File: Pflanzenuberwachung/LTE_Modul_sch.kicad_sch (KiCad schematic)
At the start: 22 parts, among them IC1 2615011136000, IC2 SN74AVC4T245PWR, J1 Antennen Anschluss, J2 Nano Sim, Q1 BSS138, SW1 CK_KMS2xxG

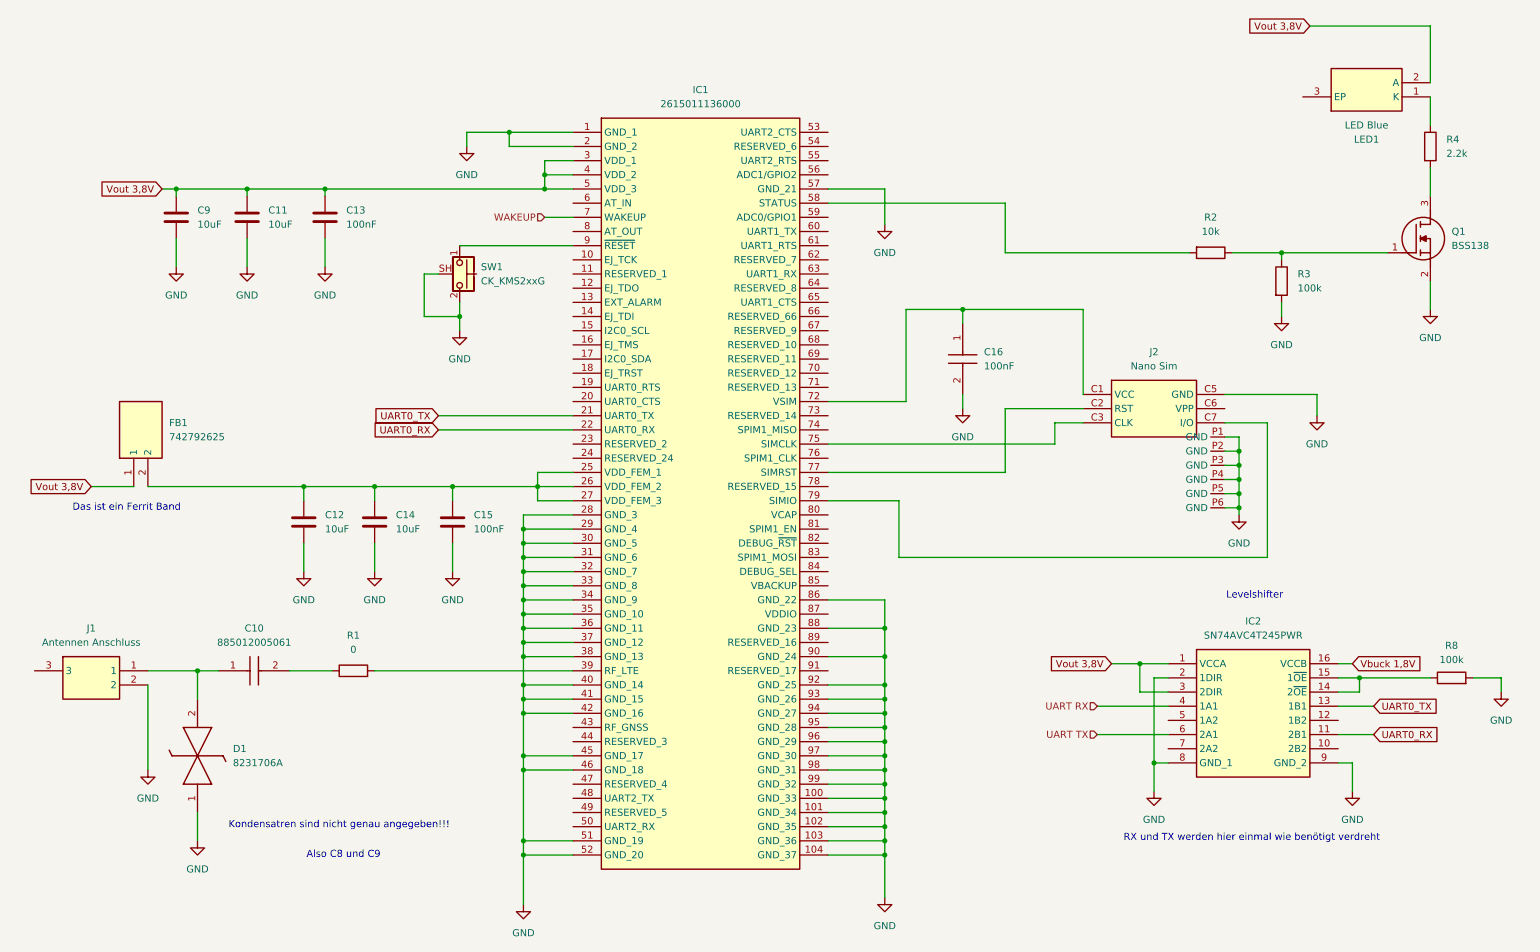
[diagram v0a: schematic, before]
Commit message: PCB Bord
PCB Design und kleiner nicht relevante änderungen
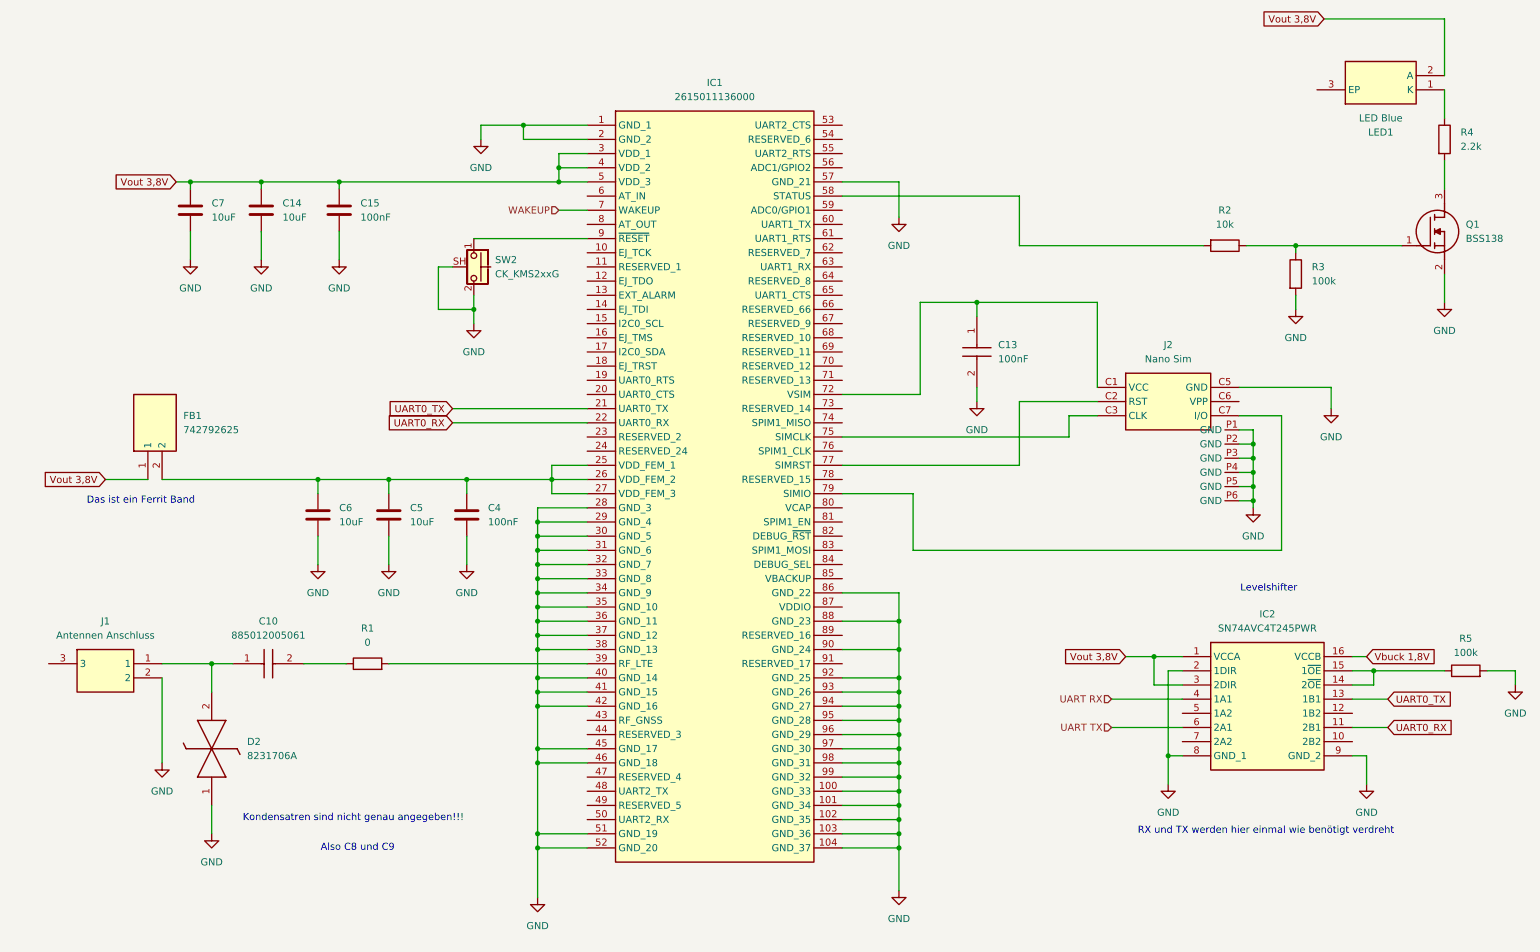
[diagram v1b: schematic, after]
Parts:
- removed C11, C12, C9: 10uF, Capacitor_SMD:C_0805_2012Metric, symbol Device:C
- removed C13: 100nF, Capacitor_SMD:C_0805_2012Metric, symbol Device:C
- removed C16: 100nF, Capacitor_SMD:C_0805_2012Metric, symbol Bauteile2:885012205037
- removed D1: 8231706A, DIONC1005X60N, symbol Bauteile2:8231706A
- removed R8: 100k, Resistor_SMD:R_0805_2012Metric, symbol Device:R
- removed SW1: CK_KMS2xxG, Button_Switch_SMD:SW_SPST_CK_KMS2xxGP, symbol Switch:CK_KMS2xxG
- added C13: 100nF, Capacitor_SMD:C_0805_2012Metric, symbol Bauteile2:885012205037
- added C4: 100nF, Capacitor_SMD:C_0805_2012Metric, symbol Device:C
- added C5, C6, C7: 10uF, Capacitor_SMD:C_0805_2012Metric, symbol Device:C
- added D2: 8231706A, DIONC1005X60N, symbol Bauteile2:8231706A
- added R5: 100k, Resistor_SMD:R_0805_2012Metric, symbol Device:R
- added SW2: CK_KMS2xxG, Button_Switch_SMD:SW_SPST_CK_KMS2xxGP, symbol Switch:CK_KMS2xxG
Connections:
- net GND: now also C13.2, C4.2, C5.2, C6.2, C7.2, D2.1 (K1), R5.2, SW2.2, SW2.SH (B)
- net Vout 3,8V: now also C14.1, C15.1, C7.1
- net at C10.1, J1.1: now also D2.2 (K2)
- net at IC2.14 (2~{OE}), IC2.15 (1~{OE}): now also R5.1
- net at IC1.72 (VSIM), J2.C1 (VCC): now also C13.1
- net at FB1.2, IC1.25 (VDD_FEM_1), IC1.26 (VDD_FEM_2)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: now also C4.1, C5.1, C6.1; no longer C14.1, C15.1
- net at IC1.9 (~{RESET}): now also SW2.1
